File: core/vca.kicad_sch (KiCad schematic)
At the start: 28 parts, among them Q10 MMBT3906, Q9 MMBT3906, U5 LM13700, U6 TL072

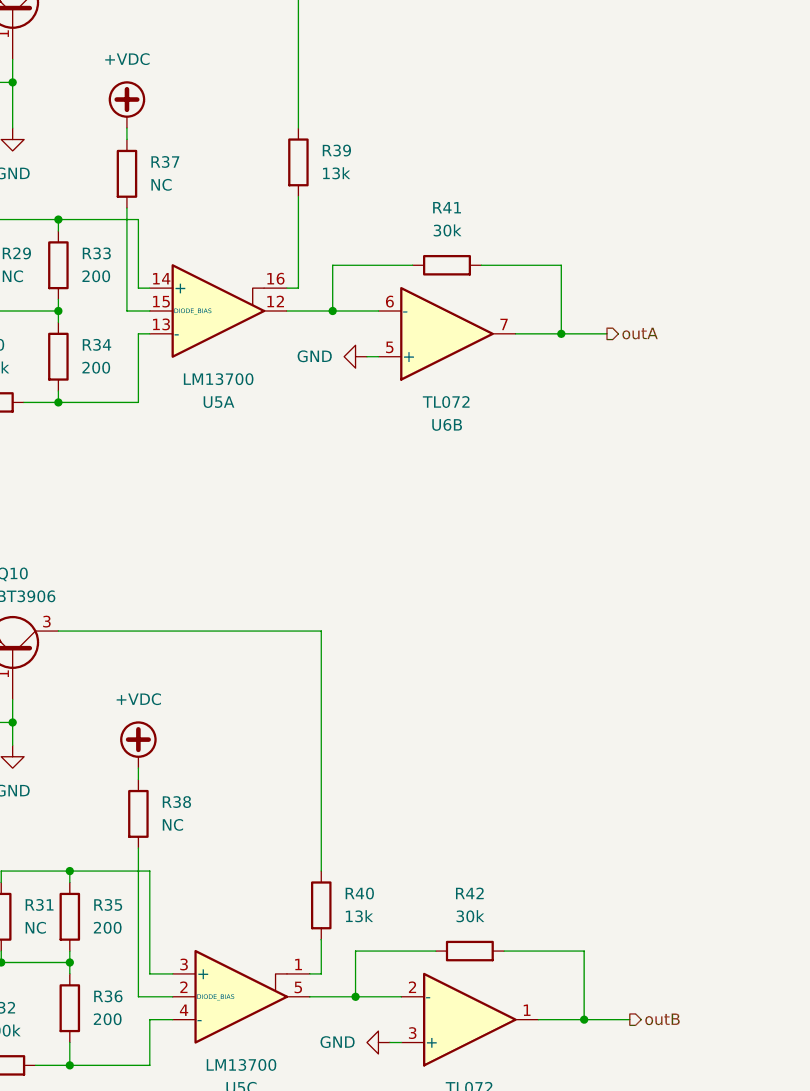
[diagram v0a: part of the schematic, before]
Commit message: Tweak resistor values
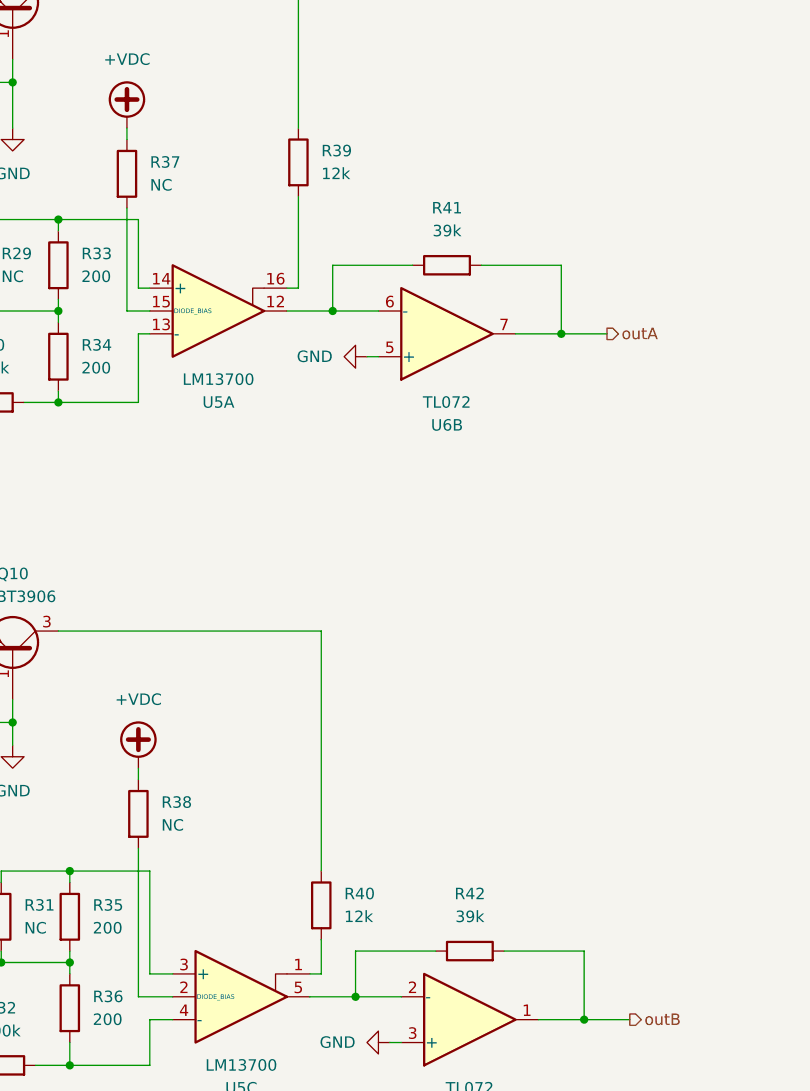
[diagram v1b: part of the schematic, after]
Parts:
- R39, R40: value 13k -> 12k
- R41, R42: value 30k -> 39k
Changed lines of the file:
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@@
 			)
 		)
-		(property "Value" "30k"
+		(property "Value" "39k"
 			(at 149.86 62.23 90)
 			(effects
@@
 			)
 		)
-		(property "Value" "13k"
+		(property "Value" "12k"
 			(at 138.43 138.4299 0)
 			(effects
@@
 			)
 		)
-		(property "Value" "13k"
+		(property "Value" "12k"
 			(at 135.89 55.8799 0)
 			(effects
@@
 			)
 		)
-		(property "Value" "30k"
+		(property "Value" "39k"
 			(at 152.4 138.43 90)
 			(effects

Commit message: Update partnames
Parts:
- D7, D8: value D -> 1N4148
- R29, R31, R37, R38: now not fitted
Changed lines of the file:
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@@
 		(in_bom yes)
 		(on_board yes)
-		(dnp no)
+		(dnp yes)
 		(fields_autoplaced yes)
 		(property "Reference" "R29"
@@
 		(in_bom yes)
 		(on_board yes)
-		(dnp no)
+		(dnp yes)
 		(fields_autoplaced yes)
 		(property "Reference" "R31"
@@
 		(in_bom yes)
 		(on_board yes)
-		(dnp no)
+		(dnp yes)
 		(fields_autoplaced yes)
 		(property "Reference" "R38"
@@
 			)
 		)
-		(property "Value" "D"
+		(property "Value" "1N4148"
 			(at 93.98 41.9099 90)
 			(effects
@@
 		(in_bom yes)
 		(on_board yes)
-		(dnp no)
+		(dnp yes)
 		(fields_autoplaced yes)
 		(property "Reference" "R37"
@@
 			)
 		)
-		(property "Value" "D"
+		(property "Value" "1N4148"
 			(at 93.98 113.0299 90)
 			(effects

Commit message: Fixes for v1.1
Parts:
- R26: renamed from R30; value 100k -> 47k
- R28: renamed from R32; value 100k -> 47k
- R35: renamed from R39; value 12k -> 39k
- R36: renamed from R40; value 12k -> 39k
- R37: renamed from R41; value 39k -> 51k
- R38: renamed from R42; value 39k -> 51k
- renumbered D7 to D5, D8 to D6, Q9 to Q10, Q10 to Q11, R25 to R21, R26 to R22, R27 to R23, R28 to R24, R29 to R25, R31 to R27, R33 to R29, R34 to R30, R35 to R31, R36 to R32, R37 to R33, R38 to R34

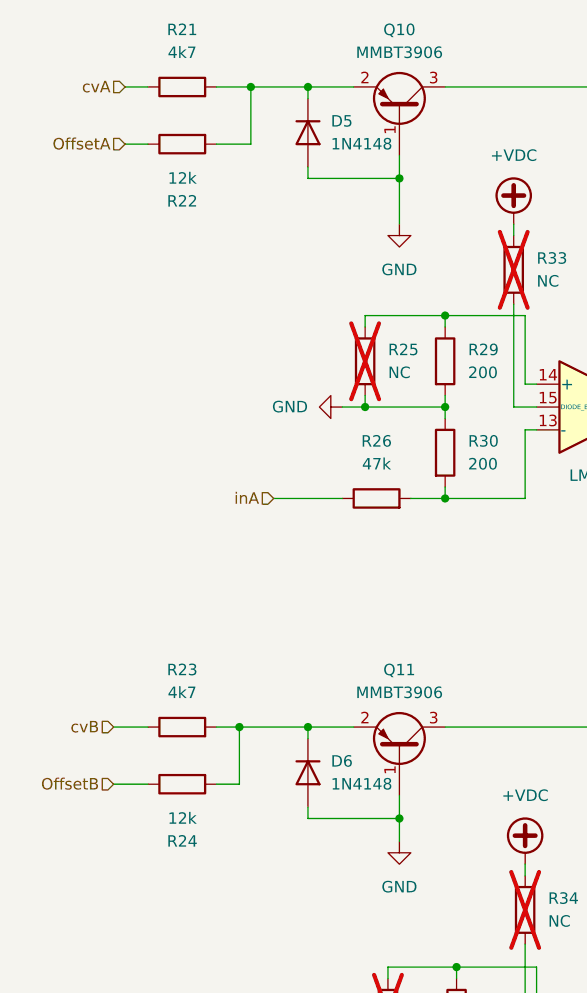
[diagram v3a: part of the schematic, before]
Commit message: Fix CV scaling for new VCA stage
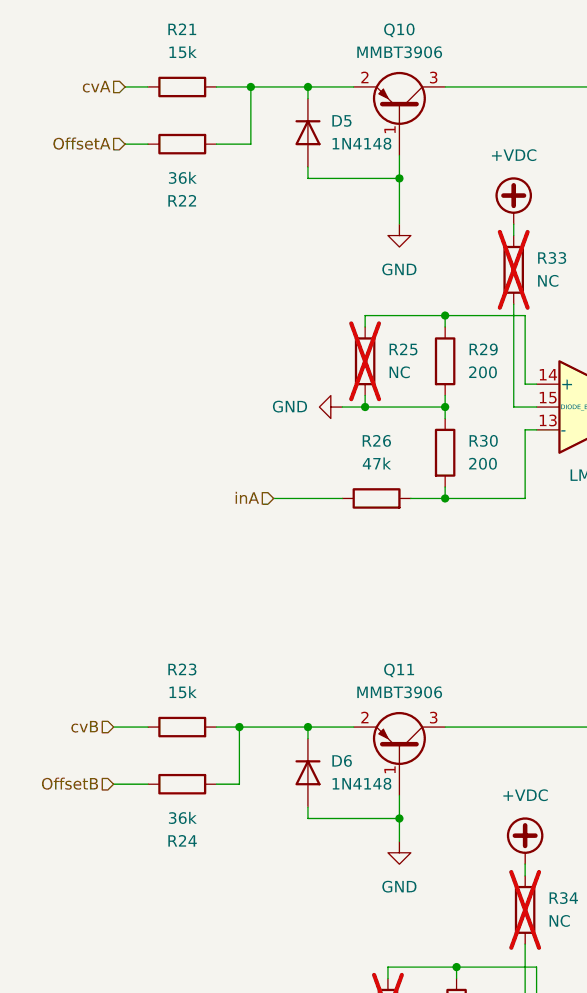
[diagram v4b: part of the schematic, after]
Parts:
- R21, R23: value 4k7 -> 15k
- R22, R24: value 12k -> 36k
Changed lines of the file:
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@@
 			)
 		)
-		(property "Value" "12k"
+		(property "Value" "36k"
 			(at 77.47 116.84 90)
 			(effects
@@
 			)
 		)
-		(property "Value" "12k"
+		(property "Value" "36k"
 			(at 77.47 45.72 90)
 			(effects
@@
 			)
 		)
-		(property "Value" "4k7"
+		(property "Value" "15k"
 			(at 77.47 102.87 90)
 			(effects
@@
 			)
 		)
-		(property "Value" "4k7"
+		(property "Value" "15k"
 			(at 77.47 31.75 90)
 			(effects
